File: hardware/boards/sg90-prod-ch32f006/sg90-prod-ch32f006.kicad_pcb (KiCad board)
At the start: 6 copper layers, 12.5 x 10 mm, 34 parts, among them J1 Servo Input, J2 Motor, J3 Debug, J4 Potentiometer, Q1 AO3401A, U1 TPAP2210K-3.3TRG1, U2 SN74LVC1G07DRLR_C19829624, U3 DRV8837DSGR-JSM, U4 CH32V006F8U6

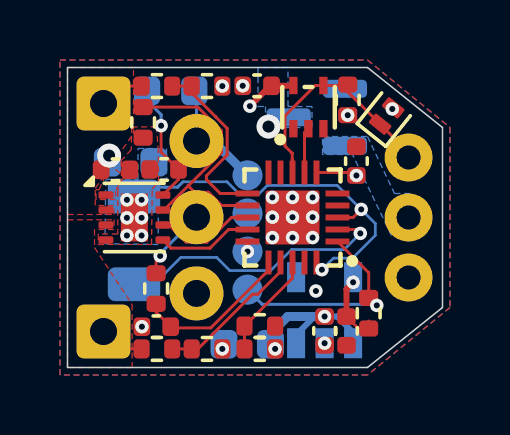
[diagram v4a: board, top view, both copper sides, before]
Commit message: better layer strategy to make signals more quite
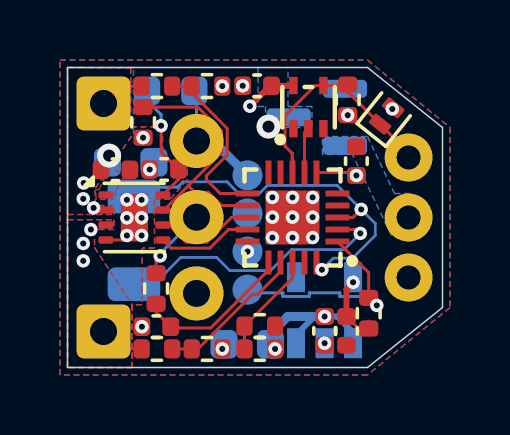
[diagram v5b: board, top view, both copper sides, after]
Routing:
- net PGND: track 0.00 -> 0.76 mm, vias 6 -> 8
- net GND: vias 16 -> 15
- net /OUTB: vias 0 -> 3
- net /OUTA: vias 0 -> 3
- added copper zone on B.Cu, net /OUTA
- added copper zone on B.Cu, net /OUTB
- added copper zone on In3.Cu, net GND
- added copper zone on In4.Cu, net GND
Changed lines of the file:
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@@
 			(remove_unused_layers yes)
 			(keep_end_layers no)
-			(zone_layer_connections "F.Cu" "In1.Cu" "B.Cu")
+			(zone_layer_connections "F.Cu" "In1.Cu" "In3.Cu" "In4.Cu" "B.Cu")
 			(net 1 "GND")
 			(pinfunction "Pin_3")
@@
 	)
 	(via
-		(at 108.28 97.45)
-		(size 0.45)
-		(drill 0.2)
-		(layers "F.Cu" "B.Cu")
-		(net 1)
-	)
-	(via
 		(at 105.16 90.62)
 		(size 0.45)
@@
 	)
 	(segment
-		(start 106.49 97.895)
+		(start 106.105 97.51)
 		(end 106 97.405)
 		(width 0.1)
@@
 	)
 	(segment
+		(start 109.961 97.581)
+		(end 109.961 97.631)
+		(width 0.1)
+		(layer "B.Cu")
+		(net 3)
+	)
+	(segment
+		(start 109.079 97.51)
+		(end 108.061 97.51)
+		(width 0.1)
+		(layer "B.Cu")
+		(net 3)
+	)
+	(segment
+		(start 108.061 97.51)
+		(end 108.061 97.631)
+		(width 0.1)
+		(layer "B.Cu")
+		(net 3)
+	)
+	(segment
+		(start 108.061 97.631)
+		(end 107.179 97.631)
+		(width 0.1)
+		(layer "B.Cu")
+		(net 3)
+	)
+	(segment
+		(start 109.079 97.631)
+		(end 109.079 97.51)
+		(width 0.1)
+		(layer "B.Cu")
+		(net 3)
+	)
+	(segment
+		(start 107.179 97.631)
+		(end 107.179 97.51)
+		(width 0.1)
+		(layer "B.Cu")
+		(net 3)
+	)
+	(segment
+		(start 109.961 97.631)
+		(end 109.079 97.631)
+		(width 0.1)
+		(layer "B.Cu")
+		(net 3)
+	)
+	(segment
 		(start 110.31 97.93)
-		(end 110.275 97.895)
+		(end 109.961 97.581)
 		(width 0.1)
 		(layer "B.Cu")
@@
 	)
 	(segment
-		(start 110.275 97.895)
-		(end 106.49 97.895)
+		(start 107.179 97.51)
+		(end 106.105 97.51)
 		(width 0.1)
 		(layer "B.Cu")
@@
 		(net 4)
 	)
+	(segment
+		(start 101.83 95.75)
+		(end 101.98 95.6)
+		(width 0.1)
+		(layer "F.Cu")
+		(net 5)
+	)
+	(segment
+		(start 101.28 95.75)
+		(end 101.83 95.75)
+		(width 0.1)
+		(layer "F.Cu")
+		(net 5)
+	)
+	(via
+		(at 102.52 92.34)
+		(size 0.45)
+		(drill 0.2)
+		(layers "F.Cu" "B.Cu")
+		(net 5)
+	)
 	(via
 		(at 101.98 95.6)
@@
 	(via
 		(at 101.98 94.41)
+		(size 0.45)
+		(drill 0.2)
+		(layers "F.Cu" "B.Cu")
+		(net 5)
+	)
+	(via
+		(at 102.74 93.4)
 		(size 0.45)
 		(drill 0.2)
@@
 		(net 7)
 	)
+	(via
+		(at 100.78 95.4)
+		(size 0.45)
+		(drill 0.2)
+		(layers "F.Cu" "B.Cu")
+		(free yes)
+		(net 7)
+	)
+	(via
+		(at 100.525 96.443965)
+		(size 0.45)
+		(drill 0.2)
+		(layers "F.Cu" "B.Cu")
+		(free yes)
+		(net 7)
+	)
+	(via
+		(at 100.525 95.86562)
+		(size 0.45)
+		(drill 0.2)
+		(layers "F.Cu" "B.Cu")
+		(free yes)
+		(net 7)
+	)
 	(segment
 		(start 102.47 90.62)
@@
 		(width 0.1)
 		(layer "F.Cu")
+		(net 8)
+	)
+	(via
+		(at 100.54 93.85)
+		(size 0.45)
+		(drill 0.2)
+		(layers "F.Cu" "B.Cu")
+		(free yes)
+		(net 8)
+	)
+	(via
+		(at 100.87 94.68)
+		(size 0.45)
+		(drill 0.2)
+		(layers "F.Cu" "B.Cu")
+		(free yes)
+		(net 8)
+	)
+	(via
+		(at 100.525 94.376649)
+		(size 0.45)
+		(drill 0.2)
+		(layers "F.Cu" "B.Cu")
+		(free yes)
 		(net 8)
 	)
@@
 	)
 	(zone
-		(net 8)
-		(net_name "/OUTA")
+		(net 28)
+		(net_name "/VSYS")
 		(layer "F.Cu")
 		(hatch edge 0.5)
-		(priority 3)
+		(priority 8)
 		(connect_pads yes
 			(clearance 0.1)
@@
 		(polygon
 			(pts
-				(xy 100 90) (xy 100 94.9) (xy 101.55 94.9) (xy 101.55 94.6) (xy 100.925 94.6) (xy 100.925 94.025)
-				(xy 102.2 92.2) (xy 102.2 90)
+				(xy 100.95 94.075) (xy 101.05 94.075) (xy 101.34 93.44) (xy 101.34 93.21) (xy 101.9 93.62) (xy 101.6 94.1)
+				(xy 101.6 94.4) (xy 100.95 94.4)
 			)
 		)
 	)
 	(zone
-		(net 7)
-		(net_name "/OUTB")
-		(layer "F.Cu")
+		(net 8)
+		(net_name "/OUTA")
+		(layers "F.Cu" "B.Cu")
 		(hatch edge 0.5)
-		(priority 4)
+		(priority 6)
 		(connect_pads yes
 			(clearance 0.1)
@@
 		(polygon
 			(pts
-				(xy 100 100) (xy 100 95.075) (xy 101.55 95.075) (xy 101.55 95.4) (xy 100.9 95.4) (xy 100.9 96) (xy 102.155 97.9)
-				(xy 102.155 100)
+				(xy 100 90) (xy 100 94.9) (xy 101.55 94.9) (xy 101.55 94.6) (xy 100.925 94.6) (xy 100.925 94.025)
+				(xy 102.2 92.2) (xy 102.2 90)
 			)
 		)
 	)
 	(zone
-		(net 5)
-		(net_name "PGND")
-		(layer "F.Cu")
+		(net 7)
+		(net_name "/OUTB")
+		(layers "F.Cu" "B.Cu")
 		(hatch edge 0.5)
-		(priority 6)
+		(priority 7)
 		(connect_pads yes
 			(clearance 0.1)
@@
 		(polygon
 			(pts
-				(xy 101.025 95.9) (xy 102.8 95.9) (xy 102.825 94.05) (xy 103.04 93.81) (xy 103.025 92.8) (xy 102.975 92.075)
-				(xy 102.975 91.975) (xy 102.14 91.983641) (xy 102.125 92.74) (xy 101.79 93.1) (xy 101.8 93.72) (xy 101.675 94.1)
-				(xy 101.675 95.55) (xy 101.025 95.55)
-			)
-		)
-	)
-	(zone
-		(net 28)
-		(net_name "/VSYS")
-		(layer "F.Cu")
-		(hatch edge 0.5)
-		(priority 5)
-		(connect_pads yes
-			(clearance 0.1)
-		)
-		(min_thickness 0.1)
-		(filled_areas_thickness no)
-		(fill yes
-			(thermal_gap 0.5)
-			(thermal_bridge_width 0.5)
-		)
-		(polygon
-			(pts
-				(xy 100.95 94.075) (xy 101.05 94.075) (xy 101.34 93.44) (xy 101.34 93.21) (xy 101.9 93.62) (xy 101.6 94.1)
-				(xy 101.6 94.4) (xy 100.95 94.4)
+				(xy 100 100) (xy 100 95.075) (xy 101.55 95.075) (xy 101.55 95.4) (xy 100.9 95.4) (xy 100.9 96) (xy 102.155 97.9)
+				(xy 102.155 100)
 			)
 		)
@@
 	)
 	(zone
-		(net 28)
-		(net_name "/VSYS")
-		(layer "B.Cu")
+		(net 5)
+		(net_name "PGND")
+		(layers "F.Cu" "B.Cu" "In3.Cu")
 		(hatch edge 0.5)
-		(priority 1)
+		(priority 5)
 		(connect_pads yes
 			(clearance 0.1)
@@
 		(polygon
 			(pts
-				(xy 106.35 90) (xy 106.35 91.3) (xy 106.6 91.3) (xy 106.6 92) (xy 108.15 92) (xy 108.15 91.3) (xy 107.35 91.3)
-				(xy 107.35 90)
+				(xy 100 90) (xy 102.11 90.01) (xy 102.11 91.98) (xy 103.16 91.975) (xy 103.18 93.1) (xy 103.99 93.08)
+				(xy 103.99 93.75) (xy 103.42 94.39) (xy 102.9 94.39) (xy 102.9 96.02) (xy 102.49 96.02) (xy 102.48 97.91)
+				(xy 102.16 97.91) (xy 102.155 100) (xy 100 100)
 			)
 		)
 	)
 	(zone
-		(net 2)
-		(net_name "VIN")
+		(net 28)
+		(net_name "/VSYS")
 		(layer "B.Cu")
 		(hatch edge 0.5)
-		(priority 2)
+		(priority 3)
 		(connect_pads yes
 			(clearance 0.1)
@@
 		(polygon
 			(pts
-				(xy 108.5 92.3) (xy 110 92.3) (xy 110.9 94.2) (xy 111.4 94.2) (xy 111.4 95.8) (xy 110.8 95.6) (xy 109.5 92.9)
-				(xy 108.5 92.9)
+				(xy 106.35 90) (xy 106.35 91.3) (xy 106.6 91.3) (xy 106.6 92) (xy 108.15 92) (xy 108.15 91.3) (xy 107.35 91.3)
+				(xy 107.35 90)
 			)
 		)
 	)
 	(zone
-		(net 5)
-		(net_name "PGND")
+		(net 2)
+		(net_name "VIN")
 		(layer "B.Cu")
 		(hatch edge 0.5)
-		(priority 7)
+		(priority 4)
 		(connect_pads yes
 			(clearance 0.1)
@@
 		(polygon
 			(pts
-				(xy 102.35 92.7) (xy 103.3 92.7) (xy 103.3 93.725) (xy 103.025 93.725) (xy 103.025 95.9) (xy 101.25 95.875)
-				(xy 101.275 93.725) (xy 102.35 93.725)
+				(xy 108.5 92.3) (xy 110 92.3) (xy 110.9 94.2) (xy 111.4 94.2) (xy 111.4 95.8) (xy 110.8 95.6) (xy 109.5 92.9)
+				(xy 108.5 92.9)
+			)
+		)
+	)
+	(zone
+		(net 0)
+		(net_name "")
+		(layer "In2.Cu")
+		(hatch edge 0.5)
+		(connect_pads
+			(clearance 0)
+		)
+		(min_thickness 0.25)
+		(filled_areas_thickness no)
+		(keepout
+			(tracks allowed)
+			(vias allowed)
+			(pads allowed)
+			(copperpour not_allowed)
+			(footprints allowed)
+		)
+		(placement
+			(enabled no)
+			(sheetname "/")
+		)
+		(fill
+			(thermal_gap 0.5)
+			(thermal_bridge_width 0.5)
+		)
+		(polygon
+			(pts
+				(xy 100 90) (xy 102.16 90) (xy 102.16 91.73) (xy 103 91.73) (xy 103.03 92.94) (xy 104.04 92.93)
+				(xy 104.06 93.87) (xy 103.82 93.87) (xy 103.83 96.25) (xy 102.06 96.26) (xy 102.09 100.01) (xy 100 100)
 			)
 		)
@@
 		(layer "In2.Cu")
 		(hatch edge 0.5)
+		(priority 1)
 		(connect_pads
 			(clearance 0.1)
@@
 	)
 	(zone
-		(net 5)
-		(net_name "PGND")
+		(net 1)
+		(net_name "GND")
 		(layer "In3.Cu")
 		(hatch edge 0.5)
-		(connect_pads
+		(priority 9)
+		(connect_pads yes
 			(clearance 0.1)
 		)
@@
 		(polygon
 			(pts
-				(xy 101.625 93.775) (xy 102.15 93.8) (xy 102.15 91.983641) (xy 103.725 91.975) (xy 103.725 96.025)
-				(xy 101.625 96.075)
+				(xy 102.2 90) (xy 102.155 100) (xy 110 100) (xy 112.5 98) (xy 112.5 92) (xy 110 90)
+			)
+		)
+	)
+	(zone
+		(net 0)
+		(net_name "")
+		(layer "In3.Cu")
+		(hatch edge 0.5)
+		(connect_pads yes
+			(clearance 0)
+		)
+		(min_thickness 0.15)
+		(filled_areas_thickness no)
+		(keepout
+			(tracks allowed)
+			(vias allowed)
+			(pads allowed)
+			(copperpour not_allowed)
+			(footprints allowed)
+		)
+		(placement
+			(enabled no)
+			(sheetname "/")
+		)
+		(fill
+			(thermal_gap 0.5)
+			(thermal_bridge_width 0.5)
+		)
+		(polygon
+			(pts
+				(xy 102.2 90) (xy 102.2 94.13) (xy 102.79 94.13) (xy 102.79 96) (xy 102.11 96) (xy 102.15 99.99)
+				(xy 102.69 100) (xy 102.69 96.56) (xy 103.11 96.55) (xy 103.08 93.89) (xy 102.52 93.89) (xy 102.52 90)
+			)
+		)
+	)
+	(zone
+		(net 1)
+		(net_name "GND")
+		(layer "In4.Cu")
+		(hatch edge 0.5)
+		(priority 10)
+		(connect_pads yes
+			(clearance 0.3)
+		)
+		(min_thickness 0.15)
+		(filled_areas_thickness no)
+		(fill yes
+			(thermal_gap 0.5)
+			(thermal_bridge_width 0.5)
+		)
+		(polygon
+			(pts
+				(xy 108.4 90) (xy 108.4 92.7) (xy 105.5 92.7) (xy 103.25 93.9) (xy 103.25 94.9) (xy 103.1 94.9)
+				(xy 103.1 95.9) (xy 102.7 96.15) (xy 102.7 96.8) (xy 106.1 98.85) (xy 107.15 97.8) (xy 109.25 97.8)
+				(xy 110.3 98.9) (xy 110.3 99.7) (xy 112.5 98) (xy 112.5 92) (xy 110 90)
 			)
 		)
@@
 		(layer "In4.Cu")
 		(hatch edge 0.5)
-		(connect_pads
+		(priority 2)
+		(connect_pads yes
 			(clearance 0.1)
 		)
@@
 		(polygon
 			(pts
-				(xy 99.751626 89.75) (xy 110.001626 89.75) (xy 112.751626 92) (xy 112.751626 98) (xy 110.001626 100.25)
-				(xy 99.751626 100.25)
-			)
-		)
+				(xy 108.15 90) (xy 108.15 92.45) (xy 105.5 92.45) (xy 102.05 94.13) (xy 102.1 96.65) (xy 106.15 99.05)
+				(xy 107.2 98) (xy 109 98) (xy 110 98.9) (xy 110 100) (xy 100 100) (xy 100 90)
+			)
+		)

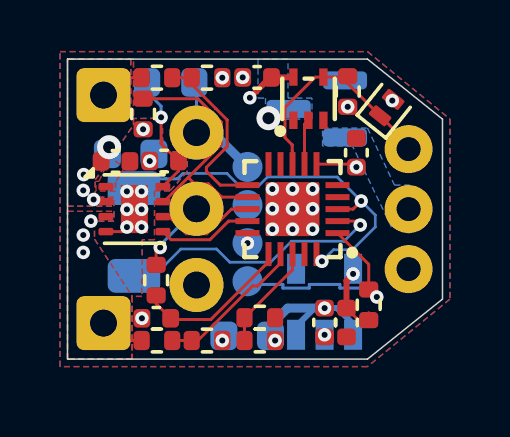
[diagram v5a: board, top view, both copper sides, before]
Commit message: added NTC thermistor since CH32V006 doesn't have internal temp sensor
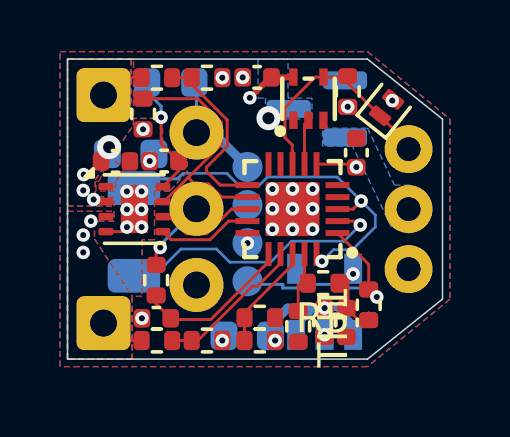
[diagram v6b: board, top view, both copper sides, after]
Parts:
- added R5: 10kΩ, Resistor_SMD:R_0402_1005Metric, F.Cu at (108.5, 97.5)
- added TH1: NTC 10k, Resistor_SMD:R_0402_1005Metric, F.Cu at (107.7, 98.9)
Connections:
- U4 pad 19: unconnected-(U4-PD5/T2/TX/RX_/MISO_/A5-Pad19) -> /VNTC
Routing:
- net /VNTC: track 0.00 -> 1.99 mm
